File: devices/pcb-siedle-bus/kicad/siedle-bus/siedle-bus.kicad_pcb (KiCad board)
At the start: 2 copper layers, 43.5 x 37 mm, 34 parts, among them J1 Conn_01x02, Q1 IRLML0030, Q2 BC807, Q3 BC807, Q4 IRLML0030, Q5 IRLML0030, SW1 RESET, SW2 BOOT, U2 ESP32-WROOM-32

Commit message: progress with siedle
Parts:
- added D2: US2MA, Diode_SMD:D_SMA, B.Cu at (158.0, 111.0)
- added R15: 10K, Resistor_SMD:R_0805_2012Metric, B.Cu at (168.5, 123.6)
- added R16: 10K, Resistor_SMD:R_0805_2012Metric, B.Cu at (160.0, 123.6)
- moved Q4 3.06 mm to (163.9, 123.5)
- moved C1 2.29 mm to (160.9, 114.0)
- moved Q5 1.12 mm to (155.9, 123.5)
- moved Q1 1.00 mm to (161.5, 104.0), turned to 180 degrees
- moved R12 1.00 mm to (164.0, 118.5)
- moved R14 1.00 mm to (168.5, 118.5)
- moved R3 0.38 mm to (162.9, 108.0)
- moved R4 0.38 mm to (158.9, 108.0)
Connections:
- net T1 renamed LOAD
- C1 pad 2: /out -> Net-(D2-A)
- Q3 pad 3: bits -> RX
- R14 pad 1: T2 -> TX
- R4 pad 2: /out -> Net-(D2-A)
- R9 pad 1: bits -> RX
- U2 pad 13: T2 -> TX
- U2 pad 28: bits -> RX
- U2 pad 34: RX -> P_RX
- U2 pad 35: TX -> P_TX
- program_port1 pad 2: TX -> P_TX
- program_port1 pad 3: RX -> P_RX
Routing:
- net bits: track 49.2 -> 0.00 mm, vias 3 -> 0
- net P_RX: track 0.00 -> 34.6 mm, vias 0 -> 2
- net P_TX: track 0.00 -> 34.0 mm, vias 0 -> 2
- net T2: track 19.3 -> 0.00 mm, vias 2 -> 0
- net TX: track 34.0 -> 20.3 mm
- net RX: track 34.6 -> 47.8 mm, vias 2 -> 3
- net Net-(D2-A): track 0.00 -> 6.63 mm
- net Net-(Q5-G): track 3.72 -> 8.00 mm
- net GND: track 194.4 -> 198.0 mm, vias 1 -> 7
- net Net-(Q4-G): track 3.78 -> 6.87 mm
- net /out: track 23.9 -> 27.0 mm
- net Net-(Q1-G): track 18.5 -> 19.8 mm
- net CARRIER: track 42.3 -> 41.3 mm
- net VBUS: track 64.9 -> 65.6 mm
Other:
- board text added: "Siedle Interphone Bus rev3 2025.7.20 Angel Nunez"
- board text removed: "Siedle Interphone Bus v1.1 2025.7.16 Angel Nunez"

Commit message: first working version working
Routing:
- net Net-(D2-A): track 6.63 -> 7.21 mm
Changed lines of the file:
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@@
 		(start 164 119.4625)
 		(end 163 120.4625)
-		(width 0.25)
+		(width 1)
 		(layer "B.Cu")
 		(net 25)
@@
 		(start 163 120.4625)
 		(end 163 123.55)
-		(width 0.25)
+		(width 1)
 		(layer "B.Cu")
 		(net 25)
@@
 		(start 155 119.5)
 		(end 155 123.55)
-		(width 0.25)
+		(width 1)
 		(layer "B.Cu")
 		(net 28)
@@
 	)
 	(segment
+		(start 157.95 109.95)
+		(end 157.95 108.95)
+		(width 1)
+		(layer "B.Cu")
+		(net 48)
+	)
+	(segment
+		(start 159 111)
+		(end 157.95 109.95)
+		(width 1)
+		(layer "B.Cu")
+		(net 48)
+	)
+	(segment
 		(start 158 108.325)
 		(end 157.95 108.375)
@@
 	(segment
 		(start 160 111)
-		(end 157.95 108.95)
-		(width 0.6)
-		(layer "B.Cu")
-		(net 48)
+		(end 159 111)
+		(width 1)
+		(layer "B.Cu")
+		(net 48)

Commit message: clean readme
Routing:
- net CARRIER: track 41.3 -> 42.6 mm
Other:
- board text added: "Siedle Interphone Bus rev4 2025.7.24 Angel Nunez"
- board text removed: "Siedle Interphone Bus rev3 2025.7.20 Angel Nunez"
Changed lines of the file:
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@@
 		)
 		(pad "2" thru_hole circle
-			(at 6.717317 0)
+			(at 6 0)
 			(size 1.6 1.6)
 			(drill 0.8)
@@
 		)
 		(embedded_fonts no)
-		(model "${KICAD9_3DMODEL_DIR}/Capacitor_THT.3dshapes/CP_Radial_Tantal_D10.5mm_P5.00mm.step"
+		(model "${KICAD9_3DMODEL_DIR}/Capacitor_THT.3dshapes/CP_Radial_D14.0mm_P5.00mm.wrl"
 			(offset
-				(xyz 0 0 0)
+				(xyz -1.2 0 0)
 			)
 			(scale
-				(xyz 1 1 1)
+				(xyz 1.5 1.5 0.5)
 			)
 			(rotate
-				(xyz 0 0 0)
+				(xyz -0 -0 -0)
 			)
 		)
@@
 		)
 		(embedded_fonts no)
-		(model "${KICAD9_3DMODEL_DIR}/Button_Switch_SMD.3dshapes/SW_SPST_PTS810.step"
+		(model "${KICAD9_3DMODEL_DIR}/Button_Switch_SMD.3dshapes/SW_SPST_PTS647Sx38.step"
 			(offset
 				(xyz 0 0 0)
 			)
 			(scale
-				(xyz 1 1 1)
+				(xyz 1 0.8 0.5)
 			)
 			(rotate
-				(xyz 0 0 0)
+				(xyz -0 -0 -0)
 			)
 		)
@@
 		)
 		(property "Value" "220uF"
-			(at 0 5.3 0)
+			(at 0 2.5 0)
 			(layer "F.Fab")
 			(effects
@@
 		)
 		(embedded_fonts no)
-		(model "${KICAD9_3DMODEL_DIR}/Button_Switch_SMD.3dshapes/SW_SPST_PTS810.step"
+		(model "${KICAD9_3DMODEL_DIR}/Button_Switch_SMD.3dshapes/SW_SPST_PTS647Sx38.step"
 			(offset
 				(xyz 0 0 0)
 			)
 			(scale
-				(xyz 1 1 1)
+				(xyz 1 0.7 0.5)
 			)
 			(rotate
-				(xyz 0 0 0)
+				(xyz -0 -0 -0)
 			)
 		)
@@
 		)
 		(property "Value" "47"
-			(at 0 -1.65 90)
+			(at -2.4625 -0.05 0)
 			(layer "B.Fab")
 			(effects
@@
 		)
 		(property "Value" "10"
-			(at 0 -1.65 0)
+			(at 2.8625 0 0)
 			(layer "B.Fab")
 			(effects
@@
 		(layer "Edge.Cuts")
 	)
-	(gr_text "Siedle Interphone Bus rev3\n2025.7.20 Angel Nunez"
+	(gr_text "Siedle Interphone Bus rev4\n2025.7.24 Angel Nunez"
 		(at 179 94.5 0)
 		(layer "F.SilkS")
@@
 	)
 	(segment
-		(start 183.02672 122.5)
-		(end 178 122.5)
+		(start 173.536068 123.463932)
+		(end 177.036068 123.463932)
 		(width 0.25)
 		(layer "F.Cu")
@@
 	)
 	(segment
-		(start 173.536068 123.463932)
-		(end 177.036068 123.463932)
+		(start 186 116.47328)
+		(end 186.503818 116.977098)
 		(width 0.25)
 		(layer "F.Cu")
@@
 	)
 	(segment
-		(start 186.5 109.5)
-		(end 186.5 116.97328)
+		(start 186 109)
+		(end 186 116.47328)
 		(width 0.25)
 		(layer "F.Cu")
@@
 	)
 	(segment
-		(start 186.5 119.02672)
-		(end 183.02672 122.5)
+		(start 183.02672 122.5)
+		(end 178 122.5)
 		(width 0.25)
 		(layer "F.Cu")
@@
 	)
 	(segment
-		(start 171.5 105)
-		(end 182 105)
+		(start 182 105)
+		(end 186 109)
 		(width 0.25)
 		(layer "F.Cu")
@@
 	)
 	(segment
-		(start 177.036068 123.463932)
-		(end 178 122.5)
+		(start 186.503818 117.578538)
+		(end 186.5 117.582356)
 		(width 0.25)
 		(layer "F.Cu")
@@
 	)
 	(segment
-		(start 186.5 116.97328)
-		(end 186.503818 116.977098)
+		(start 177.036068 123.463932)
+		(end 178 122.5)
 		(width 0.25)
 		(layer "F.Cu")
@@
 	)
 	(segment
-		(start 182 105)
-		(end 186.5 109.5)
+		(start 186.5 119.02672)
+		(end 183.02672 122.5)
 		(width 0.25)
 		(layer "F.Cu")
@@
 	)
 	(segment
-		(start 186.503818 117.578538)
-		(end 186.5 117.582356)
+		(start 171.5 105)
+		(end 182 105)
 		(width 0.25)
 		(layer "F.Cu")
@@
 	)
 	(segment
-		(start 181.63781 104)
-		(end 173 104)
+		(start 173 104)
+		(end 181.63781 104)
 		(width 0.25)
 		(layer "F.Cu")
@@
 	)
 	(segment
-		(start 187 109.36219)
-		(end 181.63781 104)
+		(start 189 111.36219)
+		(end 189 121)
 		(width 0.25)
 		(layer "F.Cu")
@@
 	)
 	(segment
-		(start 187 122)
-		(end 187 109.36219)
+		(start 181.63781 104)
+		(end 189 111.36219)
 		(width 0.25)
 		(layer "F.Cu")
@@
 	)
 	(segment
-		(start 187.5 122.5)
-		(end 187 122)
+		(start 189 121)
+		(end 187.5 122.5)
 		(width 0.25)
 		(layer "F.Cu")
@@
 		(min_thickness 0.25)
 		(filled_areas_thickness no)
-		(fill yes
+		(fill
 			(thermal_gap 0.5)
 			(thermal_bridge_width 0.5)
@@
 		(polygon
 			(pts
-				(xy 195 128) (xy 195 90.5) (xy 151.845 90.585) (xy 151.845 128)
+				(xy 195 127.5) (xy 195 90.5) (xy 151.845 90.585) (xy 151.845 127.5)
 			)
 		)

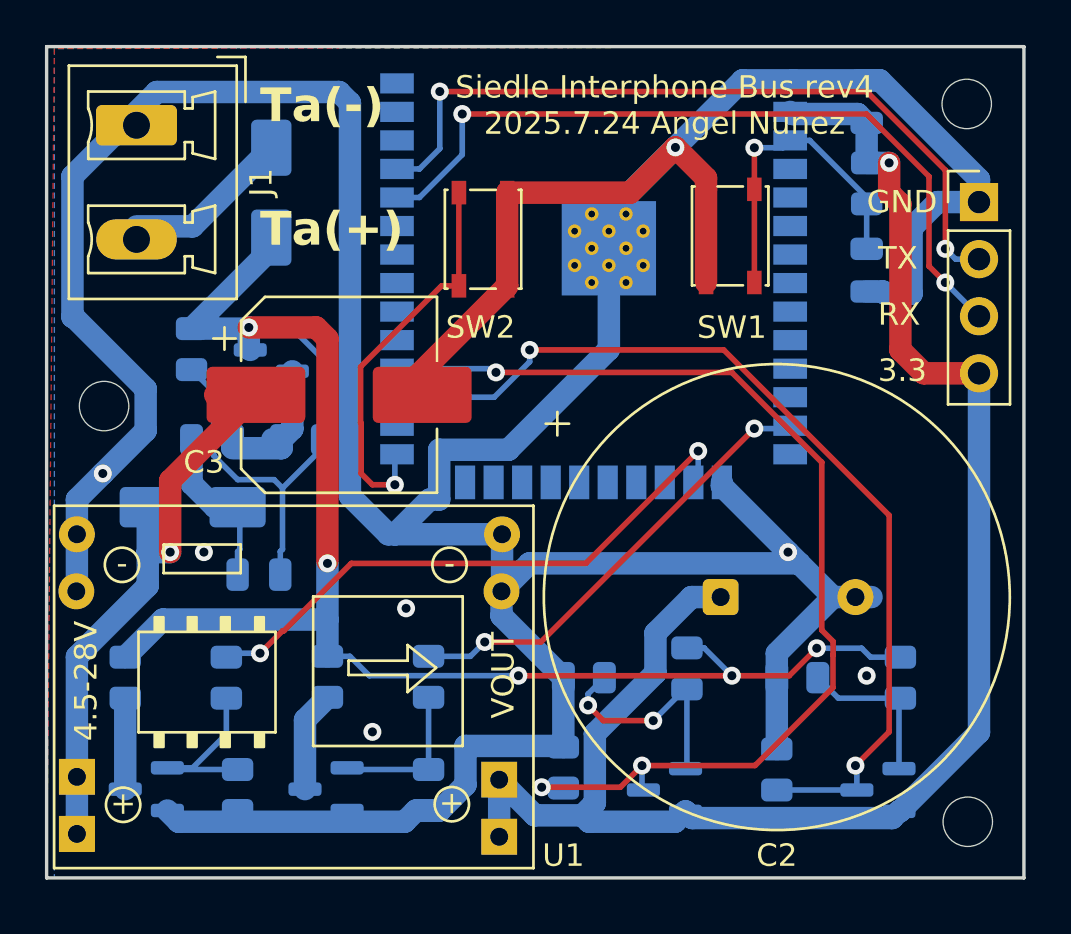
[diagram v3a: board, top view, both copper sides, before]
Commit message: add cage
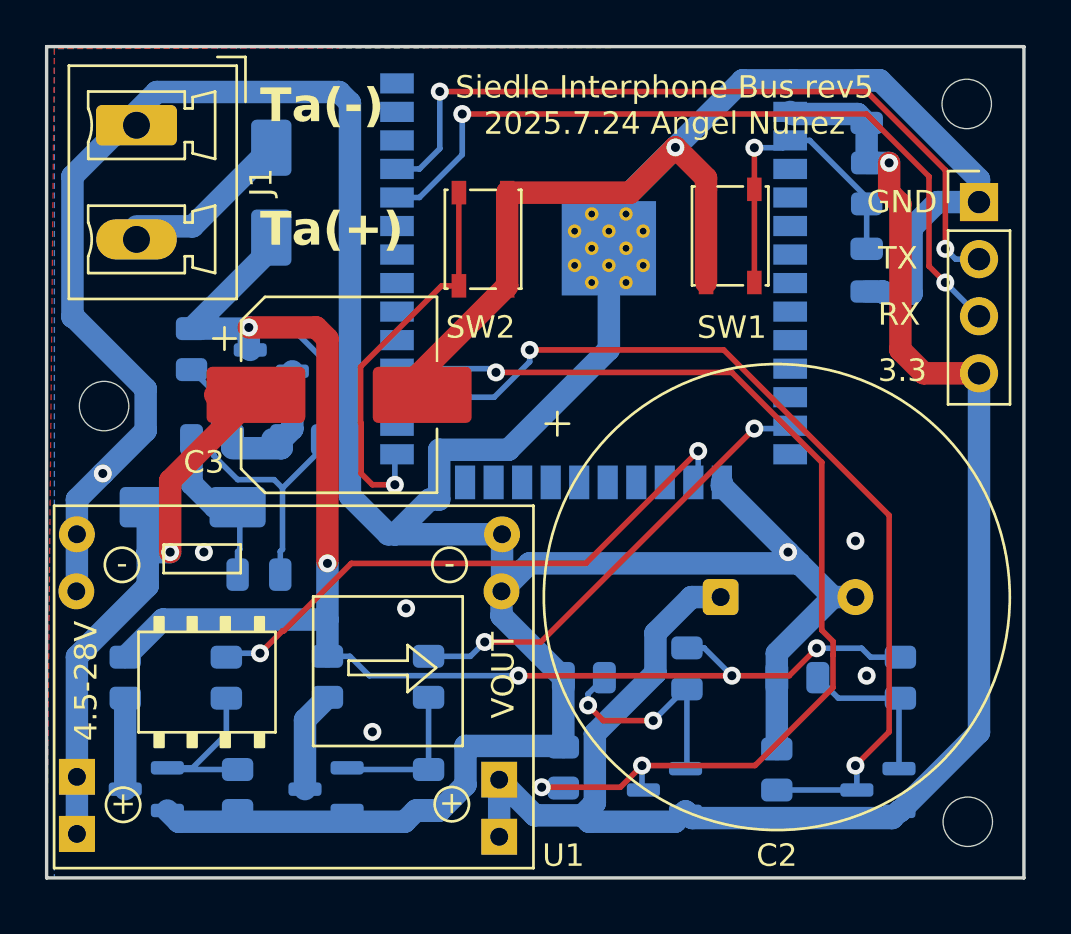
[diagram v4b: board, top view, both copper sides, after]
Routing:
- net GND: track 198.0 -> 197.3 mm, vias 7 -> 8
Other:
- board text added: "Siedle Interphone Bus rev5 2025.7.24 Angel Nunez"
- board text removed: "Siedle Interphone Bus rev4 2025.7.24 Angel Nunez"
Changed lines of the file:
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@@
 		(layer "Edge.Cuts")
 	)
-	(gr_text "Siedle Interphone Bus rev4\n2025.7.24 Angel Nunez"
+	(gr_text "Siedle Interphone Bus rev5\n2025.7.24 Angel Nunez"
 		(at 179 94.5 0)
 		(layer "F.SilkS")
@@
 		(net 3)
 	)
+	(via
+		(at 187.5 112.5)
+		(size 0.8)
+		(drill 0.4)
+		(layers "F.Cu" "B.Cu")
+		(free yes)
+		(net 3)
+	)
 	(segment
 		(start 184.5 113)
@@
 	)
 	(segment
+		(start 187.5 115)
+		(end 186.5 115)
+		(width 1)
+		(layer "B.Cu")
+		(net 3)
+	)
+	(segment
 		(start 152.649 114.5719)
 		(end 152.8226 114.7455)
@@
 		(start 182.475 92)
 		(end 179.4875 94.9875)
-		(width 1)
-		(layer "B.Cu")
-		(net 3)
-	)
-	(segment
-		(start 188.217317 115)
-		(end 186.5 115)
 		(width 1)
 		(layer "B.Cu")
@@
 		(min_thickness 0.25)
 		(filled_areas_thickness no)
-		(fill
+		(fill yes
 			(thermal_gap 0.5)
 			(thermal_bridge_width 0.5)

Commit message: update pictures
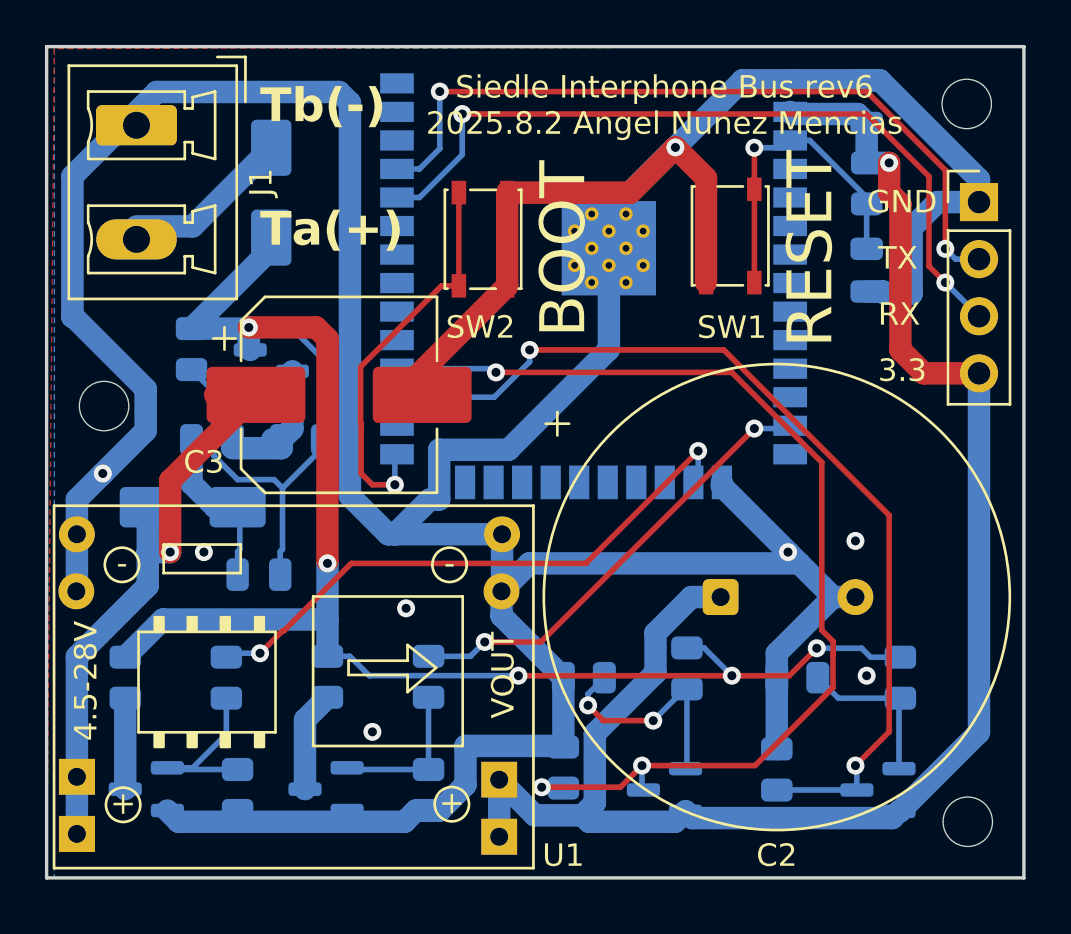
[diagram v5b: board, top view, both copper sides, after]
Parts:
- R4: value 10 -> 47
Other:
- board text added: "Siedle Interphone Bus rev6 2025.8.2 Angel Nunez Mencias"
- board text added: "Tb(-)"
- board text removed: "Siedle Interphone Bus rev5 2025.7.24 Angel Nunez"
- board text removed: "Ta(-)"
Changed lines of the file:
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@@
 		)
 		(property "Value" "RESET"
-			(at 0 2.6 90)
-			(layer "F.Fab")
+			(at -0.575 3.575 90)
+			(layer "F.SilkS")
 			(effects
 				(font
-					(size 1 1)
-					(thickness 0.15)
+					(size 2 2)
+					(thickness 0.3)
 				)
 			)
@@
 		)
 		(property "Value" "BOOT"
-			(at 0 2.6 90)
-			(layer "F.Fab")
+			(at -0.425 3.575 90)
+			(layer "F.SilkS")
 			(effects
 				(font
-					(size 1 1)
-					(thickness 0.15)
+					(size 2 2)
+					(thickness 0.3)
 				)
 			)
@@
 			)
 		)
-		(property "Value" "10"
+		(property "Value" "47"
 			(at 2.8625 0 0)
 			(layer "B.Fab")
@@
 		(layer "Edge.Cuts")
 	)
-	(gr_text "Siedle Interphone Bus rev5\n2025.7.24 Angel Nunez"
+	(gr_text "Siedle Interphone Bus rev6\n2025.8.2 Angel Nunez Mencias"
 		(at 179 94.5 0)
 		(layer "F.SilkS")
@@
 		)
 	)
-	(gr_text "Ta(-)"
+	(gr_text "Tb(-)"
 		(at 161 94 0)
 		(layer "F.SilkS")
